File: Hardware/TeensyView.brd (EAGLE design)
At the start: 35.6 x 17.8 mm, 22 parts, among them J1 DNP, J2 DNP

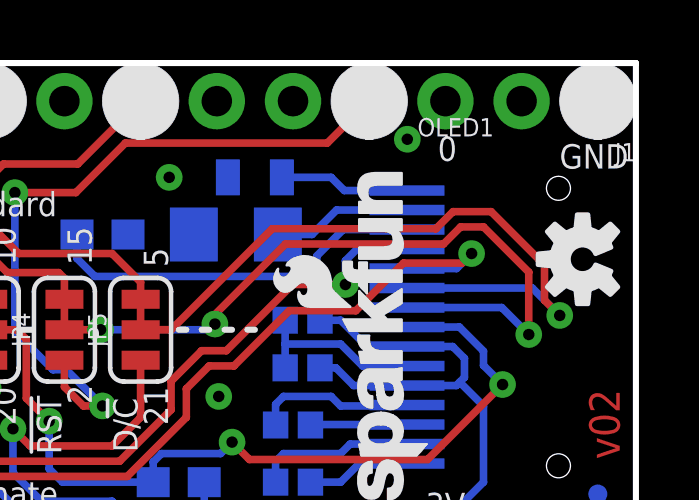
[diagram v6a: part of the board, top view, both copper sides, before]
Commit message: Added TP to OLED's VCC
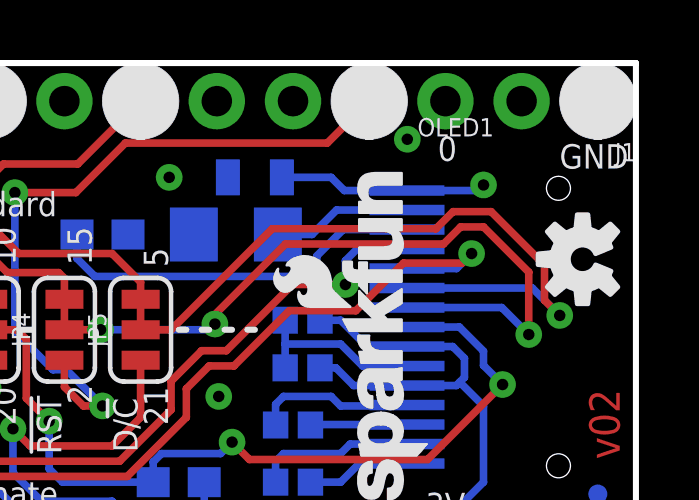
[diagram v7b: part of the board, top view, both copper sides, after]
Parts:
- added TP1: TEST-POINTTP_15TH_THRU, SparkFun-Connectors:TP_15TH
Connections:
- net N$9: now also TP1.P$1
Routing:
- net N$9: track 4.35 -> 6.98 mm
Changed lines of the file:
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@@
 <setting verticaltext="up"/>
 </settings>
-<grid distance="0.05" unitdist="inch" unit="inch" style="lines" multiple="1" display="yes" altdistance="0.0025" altunitdist="inch" altunit="inch"/>
+<grid distance="0.05" unitdist="inch" unit="inch" style="lines" multiple="1" display="yes" altdistance="0.005" altunitdist="inch" altunit="inch"/>
 <layers>
-<layer number="1" name="Top" color="4" fill="1" visible="no" active="yes"/>
+<layer number="1" name="Top" color="4" fill="1" visible="yes" active="yes"/>
 <layer number="2" name="Route2" color="1" fill="3" visible="no" active="no"/>
 <layer number="3" name="Route3" color="4" fill="3" visible="no" active="no"/>
@@
 <layer number="19" name="Unrouted" color="6" fill="1" visible="yes" active="yes"/>
 <layer number="20" name="Dimension" color="15" fill="1" visible="yes" active="yes"/>
-<layer number="21" name="tPlace" color="16" fill="1" visible="no" active="yes"/>
+<layer number="21" name="tPlace" color="16" fill="1" visible="yes" active="yes"/>
 <layer number="22" name="bPlace" color="14" fill="1" visible="yes" active="yes"/>
 <layer number="23" name="tOrigins" color="15" fill="1" visible="no" active="yes"/>
-<layer number="24" name="bOrigins" color="15" fill="1" visible="yes" active="yes"/>
+<layer number="24" name="bOrigins" color="15" fill="1" visible="no" active="yes"/>
 <layer number="25" name="tNames" color="7" fill="1" visible="no" active="yes"/>
 <layer number="26" name="bNames" color="7" fill="1" visible="no" active="yes"/>
 <layer number="27" name="tValues" color="7" fill="1" visible="no" active="yes"/>
 <layer number="28" name="bValues" color="7" fill="1" visible="no" active="yes"/>
-<layer number="29" name="tStop" color="7" fill="3" visible="yes" active="yes"/>
-<layer number="30" name="bStop" color="7" fill="6" visible="yes" active="yes"/>
-<layer number="31" name="tCream" color="7" fill="4" visible="yes" active="yes"/>
-<layer number="32" name="bCream" color="7" fill="5" visible="yes" active="yes"/>
+<layer number="29" name="tStop" color="7" fill="3" visible="no" active="yes"/>
+<layer number="30" name="bStop" color="7" fill="6" visible="no" active="yes"/>
+<layer number="31" name="tCream" color="7" fill="4" visible="no" active="yes"/>
+<layer number="32" name="bCream" color="7" fill="5" visible="no" active="yes"/>
 <layer number="33" name="tFinish" color="6" fill="3" visible="no" active="yes"/>
 <layer number="34" name="bFinish" color="6" fill="6" visible="no" active="yes"/>
@@
 <layer number="37" name="tTest" color="7" fill="1" visible="no" active="yes"/>
 <layer number="38" name="bTest" color="7" fill="1" visible="no" active="yes"/>
-<layer number="39" name="tKeepout" color="4" fill="11" visible="no" active="yes"/>
-<layer number="40" name="bKeepout" color="1" fill="11" visible="no" active="yes"/>
+<layer number="39" name="tKeepout" color="4" fill="11" visible="yes" active="yes"/>
+<layer number="40" name="bKeepout" color="1" fill="11" visible="yes" active="yes"/>
 <layer number="41" name="tRestrict" color="4" fill="10" visible="no" active="yes"/>
 <layer number="42" name="bRestrict" color="1" fill="10" visible="no" active="yes"/>
 <layer number="43" name="vRestrict" color="2" fill="10" visible="no" active="yes"/>
 <layer number="44" name="Drills" color="7" fill="1" visible="no" active="yes"/>
-<layer number="45" name="Holes" color="7" fill="1" visible="yes" active="yes"/>
+<layer number="45" name="Holes" color="7" fill="1" visible="no" active="yes"/>
 <layer number="46" name="Milling" color="3" fill="1" visible="no" active="yes"/>
 <layer number="47" name="Measures" color="7" fill="1" visible="no" active="yes"/>
@@
 <layer number="49" name="Reference" color="7" fill="1" visible="no" active="yes"/>
 <layer number="50" name="dxf" color="7" fill="1" visible="no" active="no"/>
-<layer number="51" name="tDocu" color="6" fill="1" visible="yes" active="yes"/>
+<layer number="51" name="tDocu" color="6" fill="1" visible="no" active="yes"/>
 <layer number="52" name="bDocu" color="7" fill="1" visible="no" active="yes"/>
 <layer number="53" name="tGND_GNDA" color="7" fill="9" visible="no" active="no"/>
@@
 <element name="JP4" library="SparkFun-Jumpers" package="SMT-JUMPER_3_1-NC_TRACE_SILK" value="JUMPER-SMT_3_1-NC_TRACE_SILK" x="16.51" y="8.89" rot="R90"/>
 <element name="JP5" library="SparkFun-Jumpers" package="SMT-JUMPER_3_1-NC_TRACE_SILK" value="JUMPER-SMT_3_1-NC_TRACE_SILK" x="19.05" y="8.89" rot="R90"/>
+<element name="TP1" library="SparkFun-Connectors" package="TP_15TH" value="TEST-POINTTP_15TH_THRU" x="30.48" y="13.716" rot="MR0"/>
 </elements>
 <signals>
@@
 <wire x1="25.84" y1="13.53" x2="25.4" y2="13.97" width="0.254" layer="16"/>
 <wire x1="25.4" y1="13.97" x2="23.76" y2="13.97" width="0.254" layer="16"/>
+<contactref element="TP1" pad="P$1"/>
+<wire x1="27.928" y1="13.53" x2="30.294" y2="13.53" width="0.254" layer="16"/>
+<wire x1="30.294" y1="13.53" x2="30.48" y2="13.716" width="0.254" layer="16"/>
 </signal>
 <signal name="!CS">

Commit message: worked through checklist and updated some parts, moved TP
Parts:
- C6: value 4.7UF -> 4.7uF
- OLED1: value OLED128X64SIDEREAR-MOUNT -> 32x128 OLED
- R1: value 820k -> 390k
- moved TP1 0.25 mm to (30.5, 14.0)
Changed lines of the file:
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@@
 <grid distance="0.05" unitdist="inch" unit="inch" style="lines" multiple="1" display="yes" altdistance="0.005" altunitdist="inch" altunit="inch"/>
 <layers>
-<layer number="1" name="Top" color="4" fill="1" visible="yes" active="yes"/>
+<layer number="1" name="Top" color="4" fill="1" visible="no" active="yes"/>
 <layer number="2" name="Route2" color="1" fill="3" visible="no" active="no"/>
 <layer number="3" name="Route3" color="4" fill="3" visible="no" active="no"/>
@@
 <layer number="19" name="Unrouted" color="6" fill="1" visible="yes" active="yes"/>
 <layer number="20" name="Dimension" color="15" fill="1" visible="yes" active="yes"/>
-<layer number="21" name="tPlace" color="16" fill="1" visible="yes" active="yes"/>
+<layer number="21" name="tPlace" color="16" fill="1" visible="no" active="yes"/>
 <layer number="22" name="bPlace" color="14" fill="1" visible="yes" active="yes"/>
-<layer number="23" name="tOrigins" color="15" fill="1" visible="no" active="yes"/>
-<layer number="24" name="bOrigins" color="15" fill="1" visible="no" active="yes"/>
+<layer number="23" name="tOrigins" color="15" fill="1" visible="yes" active="yes"/>
+<layer number="24" name="bOrigins" color="15" fill="1" visible="yes" active="yes"/>
 <layer number="25" name="tNames" color="7" fill="1" visible="no" active="yes"/>
 <layer number="26" name="bNames" color="7" fill="1" visible="no" active="yes"/>
@@
 <layer number="43" name="vRestrict" color="2" fill="10" visible="no" active="yes"/>
 <layer number="44" name="Drills" color="7" fill="1" visible="no" active="yes"/>
-<layer number="45" name="Holes" color="7" fill="1" visible="no" active="yes"/>
+<layer number="45" name="Holes" color="7" fill="1" visible="yes" active="yes"/>
 <layer number="46" name="Milling" color="3" fill="1" visible="no" active="yes"/>
 <layer number="47" name="Measures" color="7" fill="1" visible="no" active="yes"/>
@@
 <layer number="49" name="Reference" color="7" fill="1" visible="no" active="yes"/>
 <layer number="50" name="dxf" color="7" fill="1" visible="no" active="no"/>
-<layer number="51" name="tDocu" color="6" fill="1" visible="no" active="yes"/>
+<layer number="51" name="tDocu" color="6" fill="1" visible="yes" active="yes"/>
 <layer number="52" name="bDocu" color="7" fill="1" visible="no" active="yes"/>
 <layer number="53" name="tGND_GNDA" color="7" fill="9" visible="no" active="no"/>
@@
 <element name="LOGO2" library="SparkFun-Aesthetics" package="OSHW-LOGO-S" value="OSHW-LOGOS" x="33.782" y="11.2395" rot="R90"/>
 <element name="LOGO3" library="SparkFun-Aesthetics" package="SFE_LOGO_NAME_FLAME_.1" value="SFE_LOGO_NAME_FLAME.1_INCH" x="28.6940625" y="2.7860625" rot="R90"/>
-<element name="OLED1" library="TeensyViewDev" package="OLED-UG-2832TSWGG01-REAR" value="OLED128X64SIDEREAR-MOUNT" x="27.178" y="14.605"/>
+<element name="OLED1" library="TeensyViewDev" package="OLED-UG-2832TSWGG01-REAR" value="32x128 OLED" x="27.178" y="14.605">
+<attribute name="VALUE" value="32x128 OLED" x="27.178" y="14.605" size="1.778" layer="27" display="off"/>
+<attribute name="PROD_ID" value="LCD-13577" x="27.178" y="14.605" size="1.778" layer="27" display="off"/>
+</element>
 <element name="C1" library="SparkFun-Capacitors" package="0402" value="1.0uF" x="24.4475" y="7.62" rot="MR0">
 <attribute name="PROD_ID" value="CAP-12417" x="24.4475" y="7.62" size="1.778" layer="28" font="vector" ratio="15" rot="MR0" display="off"/>
@@
 <attribute name="PROD_ID" value="CAP-11624" x="22.86" y="13.97" size="1.778" layer="28" font="vector" ratio="15" rot="MR0" display="off"/>
 </element>
-<element name="C6" library="SparkFun-Capacitors" package="1206" value="4.7UF" x="22.225" y="12.065" rot="MR0">
+<element name="C6" library="SparkFun-Capacitors" package="1206" value="4.7uF" x="22.225" y="12.065" rot="MR0">
 <attribute name="PROD_ID" value="CAP-10300" x="22.225" y="12.065" size="1.778" layer="28" rot="MR0" display="off"/>
+<attribute name="VALUE" value="4.7uF" x="22.225" y="12.065" size="1.778" layer="28" rot="MR0" display="off"/>
 </element>
-<element name="R1" library="SparkFun-Resistors" package="0603" value="820k" x="17.78" y="12.065" rot="MR0">
-<attribute name="PROD_ID" value="RES-13247" x="17.78" y="12.065" size="1.778" layer="28" font="vector" ratio="15" rot="MR0" display="off"/>
+<element name="R1" library="SparkFun-Resistors" package="0603" value="390k" x="17.78" y="12.065" rot="MR0">
+<attribute name="PROD_ID" value="RES-12024" x="17.78" y="12.065" size="1.778" layer="28" font="vector" ratio="15" rot="MR0" display="off"/>
 </element>
 <element name="JP1" library="SparkFun-Jumpers" package="SMT-JUMPER_3_1-NC_TRACE_SILK" value="JUMPER-SMT_3_1-NC_TRACE_SILK" x="13.97" y="8.89" rot="R90"/>
@@
 <element name="JP4" library="SparkFun-Jumpers" package="SMT-JUMPER_3_1-NC_TRACE_SILK" value="JUMPER-SMT_3_1-NC_TRACE_SILK" x="16.51" y="8.89" rot="R90"/>
 <element name="JP5" library="SparkFun-Jumpers" package="SMT-JUMPER_3_1-NC_TRACE_SILK" value="JUMPER-SMT_3_1-NC_TRACE_SILK" x="19.05" y="8.89" rot="R90"/>
-<element name="TP1" library="SparkFun-Connectors" package="TP_15TH" value="TEST-POINTTP_15TH_THRU" x="30.48" y="13.716" rot="MR0"/>
+<element name="TP1" library="SparkFun-Connectors" package="TP_15TH" value="TEST-POINTTP_15TH_THRU" x="30.48" y="13.97" rot="MR0"/>
 </elements>
 <signals>
@@
 <wire x1="25.4" y1="13.97" x2="23.76" y2="13.97" width="0.254" layer="16"/>
 <contactref element="TP1" pad="P$1"/>
-<wire x1="27.928" y1="13.53" x2="30.294" y2="13.53" width="0.254" layer="16"/>
-<wire x1="30.294" y1="13.53" x2="30.48" y2="13.716" width="0.254" layer="16"/>
+<wire x1="27.928" y1="13.53" x2="30.04" y2="13.53" width="0.254" layer="16"/>
+<wire x1="30.04" y1="13.53" x2="30.48" y2="13.97" width="0.254" layer="16"/>
 </signal>
 <signal name="!CS">
